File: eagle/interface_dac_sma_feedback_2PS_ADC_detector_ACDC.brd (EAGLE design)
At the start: 158.8 x 119.4 mm, 26 parts

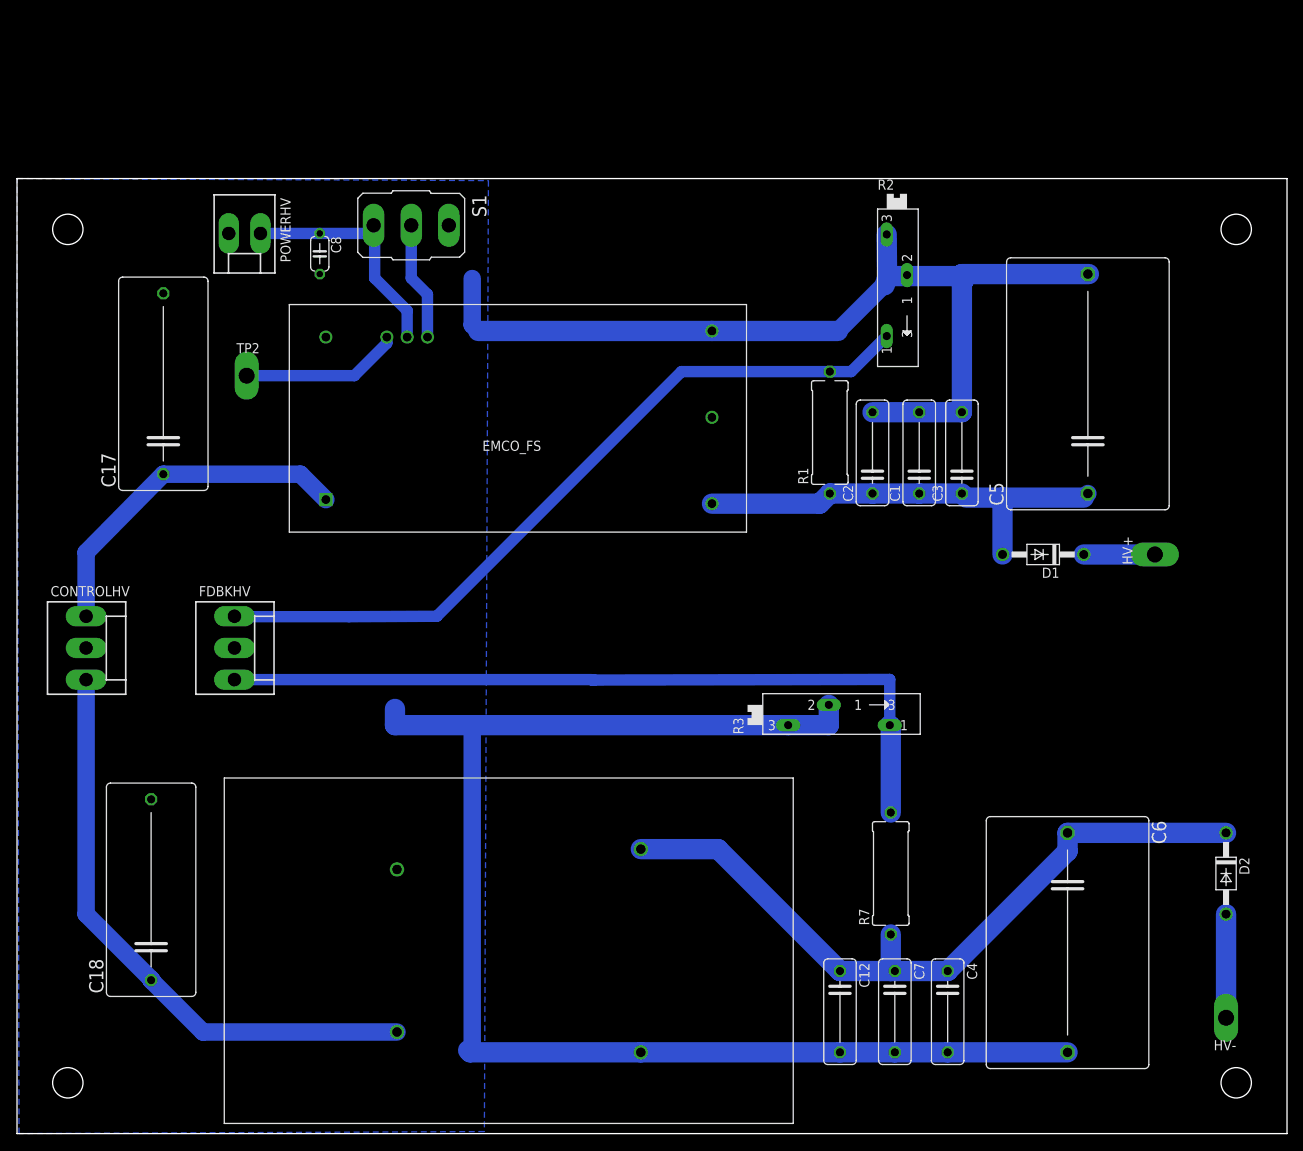
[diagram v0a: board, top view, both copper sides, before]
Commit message: Square wave one side/dc other
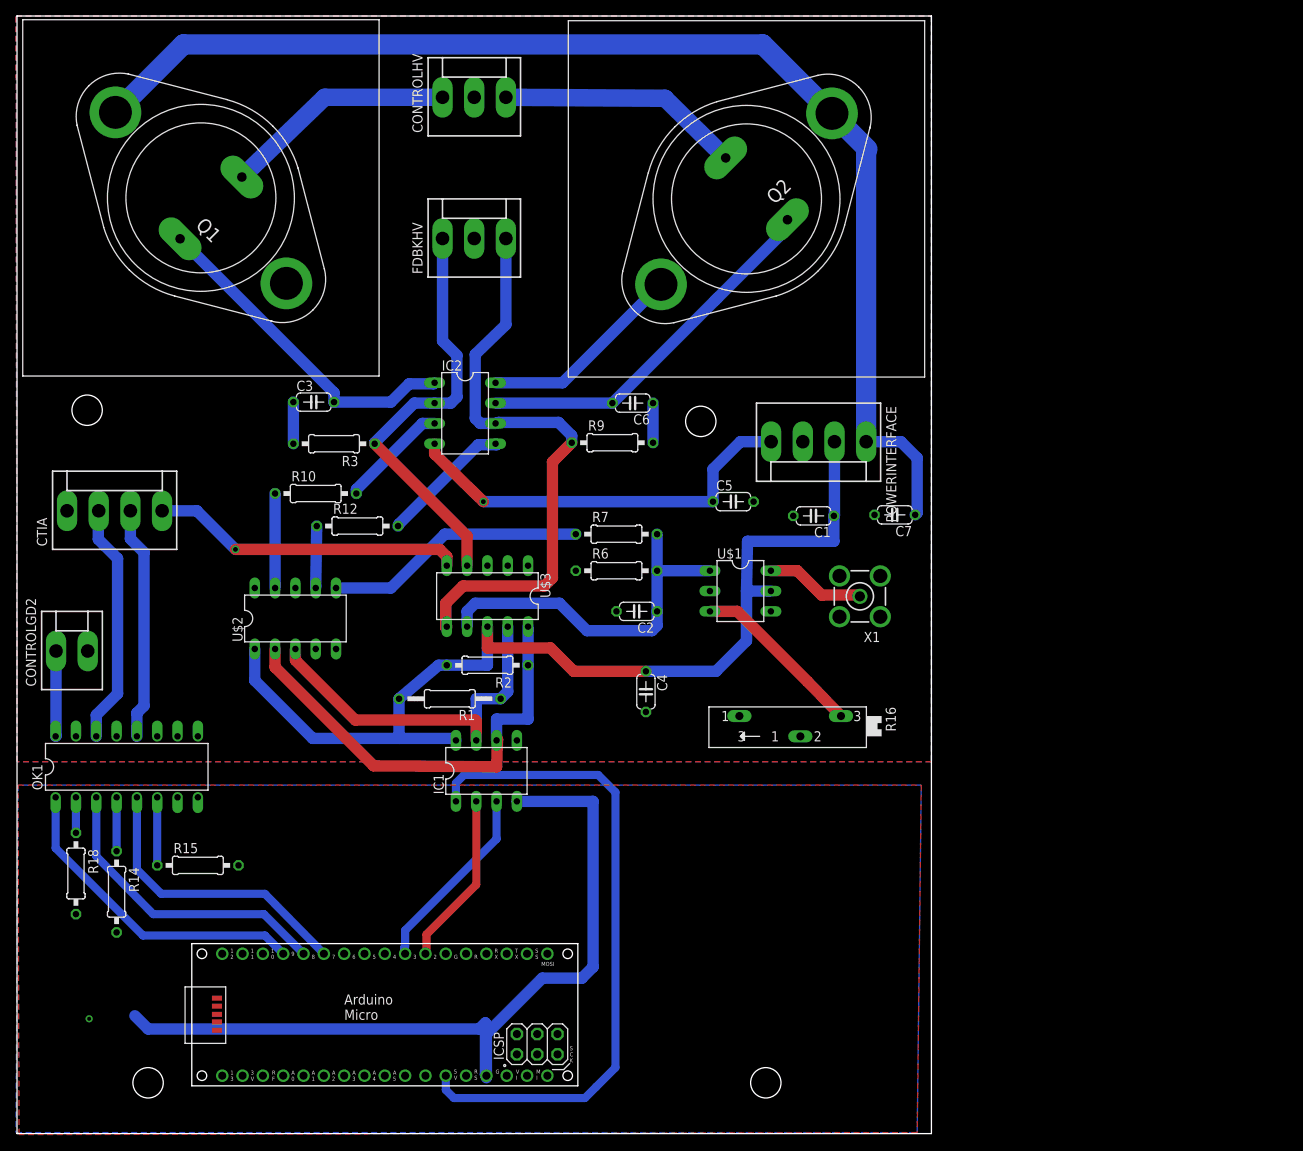
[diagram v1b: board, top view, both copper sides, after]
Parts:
- removed C12: .01u, rcl:C102-043X133
- removed C17, C18: .1u, rcl:C225-113X268
- removed C8: 10n, rcl:C050-024X044
- removed D1, D2: 1N4004, diode:DO41-10
- removed HV+, HV-: TPPAD1-20Y, testpad:P1-20Y
- removed POWERHV: (no value), con-molex:KK-156-2
- removed S1: (no value), switch:M9040P
- removed TP2: PTR1PAD1-20Y, testpad:P1-20Y
- added CONTROLGD2: (no value), con-molex:KK-156-2
- added CTIA, POWERINTERFACE: (no value), con-molex:KK-156-4
- added IC1: ISO1540, texas:DIL08
- added IC2: LT1352PA, linear-technology:DIL08
- added OK1: PS2501", optocoupler:DIL16
- added PCB1: ARDUINO_MICRO, E14_Arduino_published:ARDUINO_MICRO
- added Q1, Q2: 2N3055, transistor-npn:TO3
- added R10, R12, R6, R9: 10k, resistor:0207/10
- added R14, R15, R18: 100, rcl:0207/10
- added R16: 100k, pot:SP19L
- added U$3: ADS1015DIL, texas:DIL10
- added X1: BU-SMA-V, con-coax:BU-SMA-V
- C1: value 1n -> 10n; device rcl:C102-043X133 -> rcl:C050-024X044
- C2, C7: value 10p -> 10n; device rcl:C102-043X133 -> resistor:C050-024X044
- C3: value .01u -> 10n; device rcl:C102-043X133 -> resistor:C050-024X044
- C4: value 1n -> 10n; device rcl:C102-043X133 -> resistor:C050-024X044
- C5, C6: value 1u -> 10n; device rcl:C275-205X316 -> resistor:C050-024X044
- R1: value 2M -> 10k; device resistor:P0613/15 -> resistor:0207/12
- R2, R3: value (none) -> 10k; device pot:SP19L -> resistor:0207/10
- R7: value 2M -> 40k; device resistor:P0613/15 -> resistor:0207/10
- U$1: value EMCO-FS10 -> LTC6992; device dc-dc-converter:EMCO-FS -> linear-technology:DIL06
- U$2: value EMCO-F104PIN -> MCP4728DIL; device dc-dc-converter:EMCO-F -> microchip:DIL10
- moved C6 86.6 mm to (77.0, 91.3), turned to 180 degrees
- moved CONTROLHV 84.2 mm to (57.1, 129.5), turned to 0 degrees
- moved C3 81.3 mm to (37.1, 91.4), turned to 0 degrees
- moved R3 72.2 mm to (39.6, 86.2), turned to 180 degrees
- moved R2 69.4 mm to (58.8, 58.5), turned to 180 degrees
- moved C7 62.1 mm to (109.7, 77.3), turned to 180 degrees
- moved FDBKHV 59.3 mm to (57.1, 111.9), turned to 0 degrees
- moved R1 58.0 mm to (54.1, 54.4), turned to 180 degrees
- moved U$1 56.9 mm to (90.4, 67.8), turned to 270 degrees
- moved C4 55.0 mm to (78.6, 55.2)
- moved R7 54.5 mm to (74.9, 74.9), turned to 0 degrees
- moved U$2 53.2 mm to (34.8, 64.4)
- moved C5 46.7 mm to (89.5, 79.0), turned to 0 degrees
- moved C2 35.5 mm to (77.5, 65.3), turned to 180 degrees
- moved C1 15.4 mm to (99.6, 77.2), turned to 180 degrees
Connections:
- removed net +5V: C8.1, POWERHV.1, S1.3, U$1.+5
- removed net N$10: TP2.TP, U$1.ALARM
- removed net N$15: C18.1, CONTROLHV.3, U$2.P$1
- removed net N$8: FDBKHV.3, R3.A, R7.2
- new net +15V: C7.1, IC2.8, POWERINTERFACE.1, Q1.C, Q1.C/, Q2.C, Q2.C/
- new net -15V: C5.1, IC2.4, POWERINTERFACE.4
- new net A+5: IC1.1, PCB1.+5V
- new net AGND: IC1.4, PCB1.GND., R14.2, R15.2, R18.2
- new net CTIA: CTIA.4, U$3.5
- new net D10: PCB1.D10
- new net D11: PCB1.D11
- new net D4: PCB1.D4
- new net D7: OK1.5, PCB1.D7
- new net D8: OK1.3, PCB1.D8
- new net ENSW2: CONTROLGD2.1, OK1.16
- new net N$12: R16.E, U$1.SET
- new net N$16: IC2.3, R10.2
- new net N$18: IC2.5, R12.2
- new net N$19: C3.2, IC2.1, Q1.B
- new net N$20: C6.1, R9.2
- new net N$21: C6.2, IC2.7, Q2.B
- new net N$24: R10.1, U$2.9
- new net N$25: R12.1, U$2.7
- new net N$26: U$2.8
- new net N$7: OK1.2, R18.1
- new net PWM5: PCB1.D5
- new net PWM6: PCB1.D6
- new net PWM9: OK1.1, PCB1.D9
- new net RDBK1: FDBKHV.1, IC2.2, R3.1, U$3.4
- new net RDBK3: FDBKHV.3, IC2.6, R9.1, U$3.6
- new net RDBK4: C2.1, R6.2, R7.2, U$1.MOD, U$3.7
- new net RESET: CTIA.3, OK1.12
- new net SAMPLE: CTIA.2, OK1.14
- new net SCL: IC1.3, PCB1.D3
- new net SCL_OUT: IC1.6, R2.1, U$2.2, U$3.10
- new net SDA: IC1.2, PCB1.D2
- new net SDA_OUT: IC1.7, R1.1, U$2.3, U$3.9
- new net VCC: C1.1, C4.1, IC1.8, POWERINTERFACE.2, R1.2, R2.2, U$1.VCC, U$2.1, U$3.8
- net GND: now also CONTROLGD2.2, CTIA.1, IC1.5, OK1.11, OK1.13, OK1.15, POWERINTERFACE.3, R16.A, R16.S, R6.1, U$1.DIV, U$1.GND, U$2.10, U$2.4, U$3.1, U$3.3, X1.2, X1.3, X1.4, X1.5; no longer C12.2, C17.2, C18.2, C3.2, C6.2, C8.2, POWERHV.2, R2.E, R2.S, R3.E, R3.S, S1.1, U$1.-IN, U$1.-OUT, U$2.P$2, U$2.P$3
- net N$1: now also R7.1, U$2.6; no longer C1.1, C2.1, C3.1, C5.1, D1.A, R1.1, U$1.+OUT
- net N$13: now also U$1.OUT, X1.1; no longer C17.1, CONTROLHV.1, U$1.+IN
- net N$2: now also OK1.4, R14.1; no longer C12.1, C4.1, C6.1, C7.1, D2.C, R7.1, U$2.P$4
- net N$3: now also C3.1, R3.2; no longer FDBKHV.1, R1.2, R2.A
- net N$4: now also CONTROLHV.1, Q1.E; no longer D2.A, HV-.TP
- net N$5: now also CONTROLHV.3, Q2.E; no longer S1.2, U$1.DISABLE
- net N$6: now also OK1.6, R15.1; no longer D1.C, HV+.TP
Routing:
- net GND: track 340.8 -> 0.00 mm
- net +15V: track 0.00 -> 179.8 mm
- net VCC: track 0.00 -> 131.2 mm
- net AGND: track 0.00 -> 104.0 mm, vias 0 -> 1
- net N$8: track 98.9 -> 0.00 mm
- net N$3: track 96.1 -> 5.21 mm
- net N$2: track 92.5 -> 6.73 mm
- net A+5: track 0.00 -> 82.9 mm
- net N$15: track 74.5 -> 0.00 mm
- net RDBK3: track 0.00 -> 73.8 mm
- net SCL_OUT: track 0.00 -> 56.8 mm
- net RDBK1: track 0.00 -> 53.4 mm
- net -15V: track 0.00 -> 51.3 mm, vias 0 -> 1
- net SDA_OUT: track 0.00 -> 47.2 mm
- net N$21: track 0.00 -> 46.6 mm
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- added copper zone on layer 1, net AGND
- added copper zone on layer 16, net AGND
- added copper zone on layer 1, net GND
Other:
- board size 158.8 x 119.4 mm -> 114.3 x 139.7 mm
